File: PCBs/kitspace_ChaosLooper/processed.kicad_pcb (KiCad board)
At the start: 2 copper layers, 136.5 x 67.2 mm, 33 parts, among them J1 IN, J2 OUT, SW1 Switch, SW2 Switch, U1 PT2399

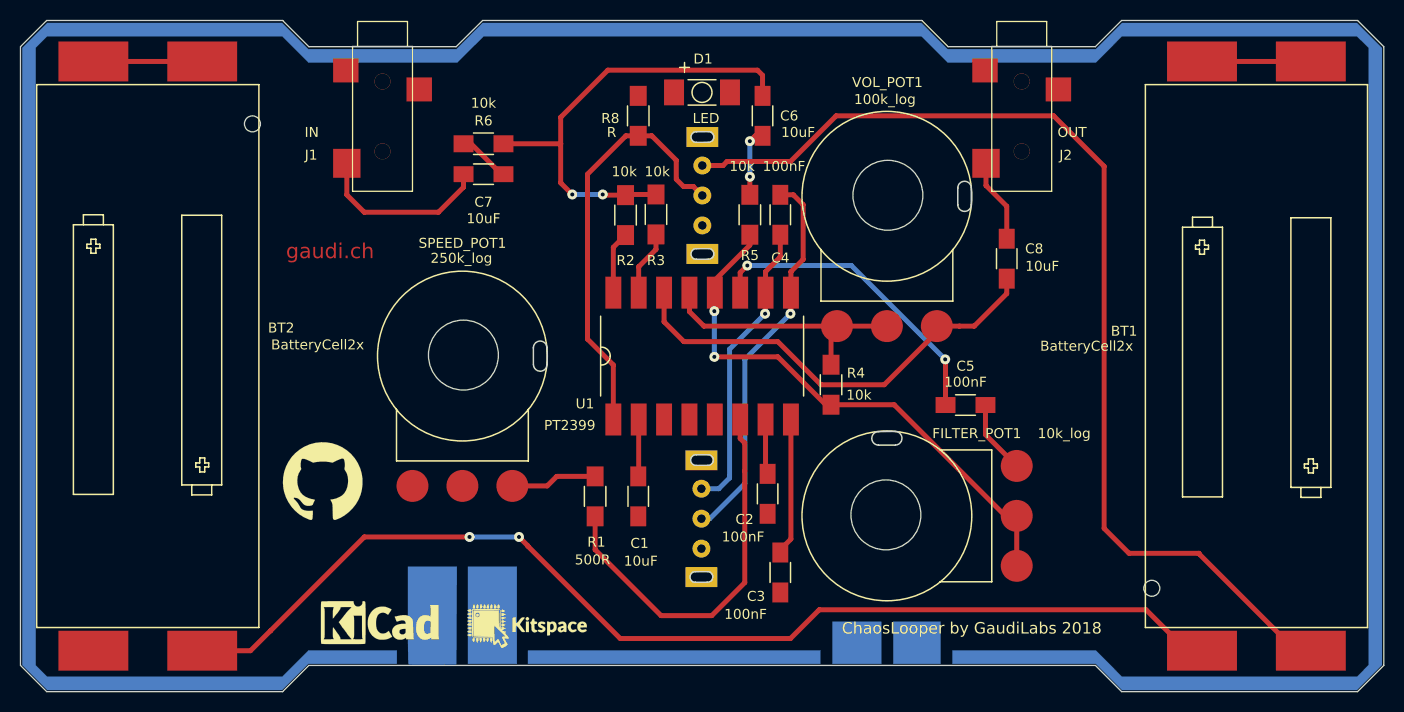
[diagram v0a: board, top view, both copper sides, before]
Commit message: recheck all circuits and clean up fill zone by rerouting the nets using freerouting and manually
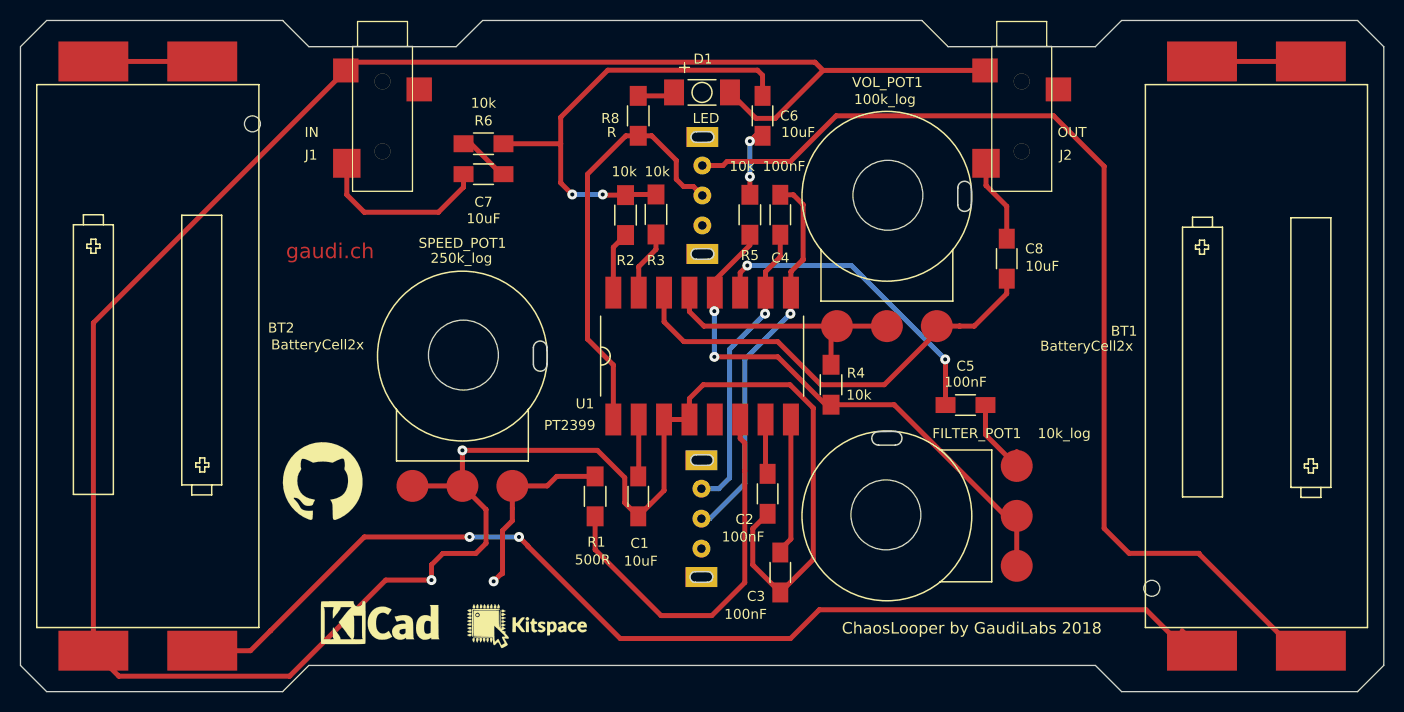
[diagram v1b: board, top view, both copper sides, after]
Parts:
- removed the G*** at (140.0, 100.0)
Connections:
- BT2 pad 4: (no net) -> GND
- C1 pad 2: (no net) -> GND
- C2 pad 1: (no net) -> GND
- C3 pad 1: (no net) -> GND
- D1 pad 1: (no net) -> GND
- D1 pad 2: (no net) -> Net-(D1-Pad2)
- J1 pad 1: (no net) -> GND
- J1 pad 2: (no net) -> Net-(J1-Pad2)
- J2 pad 1: (no net) -> GND
- J2 pad 2: (no net) -> Net-(J2-Pad2)
- R8 pad 1: (no net) -> Net-(D1-Pad2)
- SPEED_POT1 pad 2: (no net) -> GND
- SPEED_POT1 pad 3: (no net) -> GND
- SW1 pad 3: (no net) -> Net-(SW1-Pad3)
- SW2 pad 3: (no net) -> Net-(SW2-Pad3)
- U1 pad 3: (no net) -> GND
- U1 pad 4: (no net) -> GND
- U1 pad 5: (no net) -> Net-(U1-Pad5)
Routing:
- net GND: track 0.00 -> 288.6 mm, vias 0 -> 2
- net Net-(R1-Pad1): track 8.68 -> 19.1 mm, vias 0 -> 1
- net Net-(D1-Pad2): track 0.00 -> 3.64 mm
- net Net-(BT1-Pad2): track 111.9 -> 114.8 mm
- net Net-(C5-Pad1): track 7.39 -> 8.84 mm

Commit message: clean psbc that are missed before
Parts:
- renumbered G*** to G***_2, G*** to G***_3, G*** to G***_4, G*** to G***_5
